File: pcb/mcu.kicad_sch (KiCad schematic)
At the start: 28 parts, among them J1 CON_SAMTEC_14P_2R_1m27_P_KEY_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, U3 IC_MCU_STM32F100C4T6B_48LQFP, X1 XTAL_8M_20PPM_18pF_ECS-80-18-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, X2 XTAL_32K768_10PPM_7pF_ECS-.32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

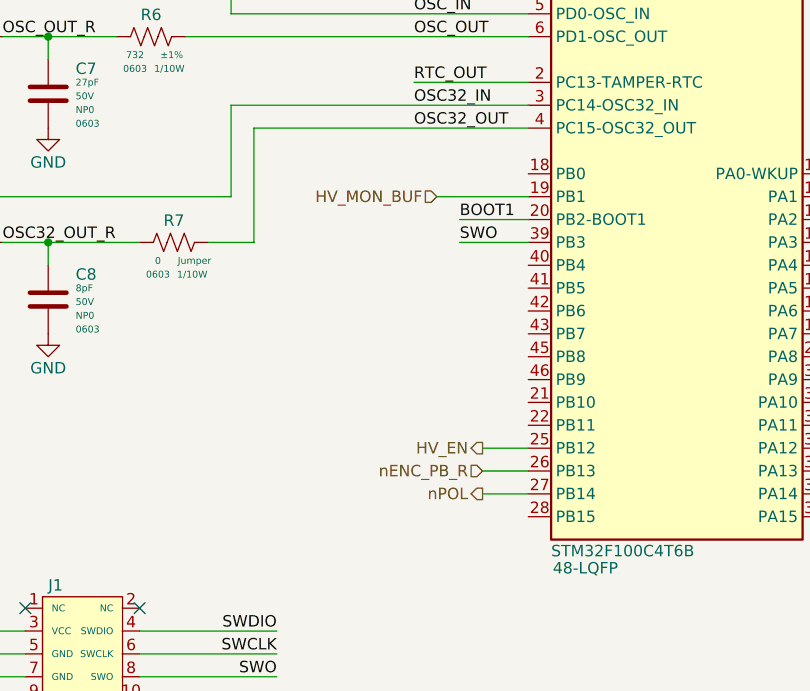
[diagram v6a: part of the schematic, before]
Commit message: Added 12V and 180V sense lines
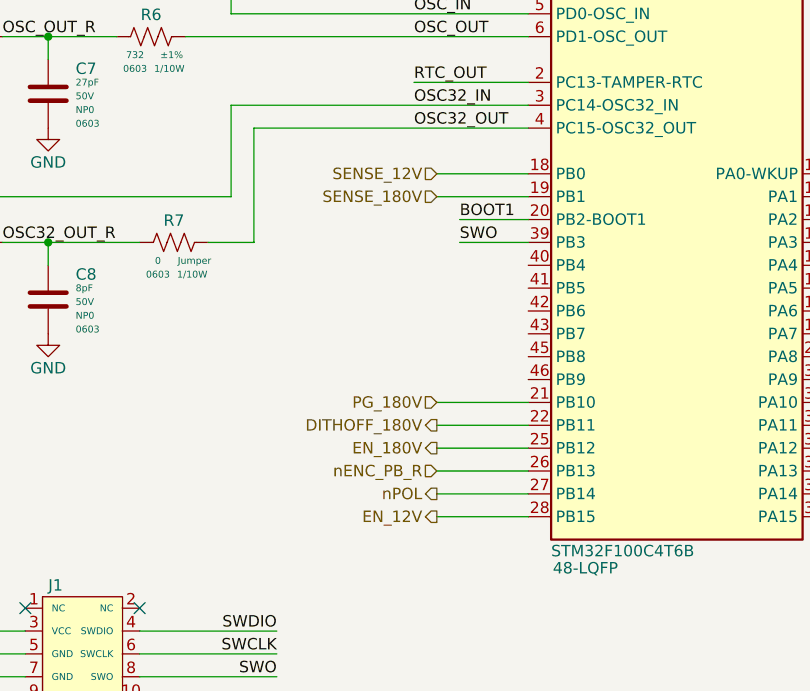
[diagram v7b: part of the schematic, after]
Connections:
- net SENSE_12V: now reaches U3.18 (PB0)
- net PG_180V: now reaches U3.21 (PB10)
- net DITHOFF_180V: now reaches U3.22 (PB11)
- net EN_12V: now reaches U3.28 (PB15)
- net HV_EN renamed EN_180V
- net HV_MON_BUF renamed SENSE_180V
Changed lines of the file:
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@@
+    (stroke (width 0) (type default) (color 0 0 0 0))
+  )
+  (wire (pts (xy 91.44 149.86) (xy 101.6 149.86))
     (stroke (width 0) (type default) (color 0 0 0 0))
   )
@@
     (stroke (width 0) (type default) (color 0 0 0 0))
   )
-  (wire (pts (xy 96.52 142.24) (xy 101.6 142.24))
+  (wire (pts (xy 91.44 142.24) (xy 101.6 142.24))
     (stroke (width 0) (type default) (color 0 0 0 0))
   )
@@
     (stroke (width 0) (type default) (color 0 0 0 0))
   )
+  (wire (pts (xy 101.6 139.7) (xy 91.44 139.7))
+    (stroke (width 0) (type default) (color 0 0 0 0))
+  )
+  (wire (pts (xy 101.6 111.76) (xy 91.44 111.76))
+    (stroke (width 0) (type default) (color 0 0 0 0))
+  )
   (wire (pts (xy 27.94 165.1) (xy 45.72 165.1))
     (stroke (width 0) (type default) (color 0 0 0 0))
@@
     (stroke (width 0) (type default) (color 0 0 0 0))
   )
-  (wire (pts (xy 96.52 147.32) (xy 101.6 147.32))
+  (wire (pts (xy 91.44 147.32) (xy 101.6 147.32))
     (stroke (width 0) (type default) (color 0 0 0 0))
   )
@@
     (stroke (width 0) (type default) (color 0 0 0 0))
   )
+  (wire (pts (xy 101.6 137.16) (xy 91.44 137.16))
+    (stroke (width 0) (type default) (color 0 0 0 0))
+  )
   (wire (pts (xy 27.94 167.64) (xy 45.72 167.64))
     (stroke (width 0) (type default) (color 0 0 0 0))
@@
     (stroke (width 0) (type default) (color 0 0 0 0))
   )
-  (wire (pts (xy 96.52 144.78) (xy 101.6 144.78))
+  (wire (pts (xy 91.44 144.78) (xy 101.6 144.78))
     (stroke (width 0) (type default) (color 0 0 0 0))
   )
@@
     (effects (font (size 1.27 1.27)) (justify left))
   )
+  (hierarchical_label "EN_12V" (shape output) (at 91.44 149.86 180)
+    (effects (font (size 1.27 1.27)) (justify right))
+  )
+  (hierarchical_label "SENSE_12V" (shape input) (at 91.44 111.76 180)
+    (effects (font (size 1.27 1.27)) (justify right))
+  )
   (hierarchical_label "PWM_nBL" (shape output) (at 152.4 127 0)
     (effects (font (size 1.27 1.27)) (justify left))
   )
-  (hierarchical_label "HV_EN" (shape output) (at 96.52 142.24 180)
+  (hierarchical_label "EN_180V" (shape output) (at 91.44 142.24 180)
     (effects (font (size 1.27 1.27)) (justify right))
   )
@@
     (effects (font (size 1.27 1.27)) (justify left))
   )
-  (hierarchical_label "HV_MON_BUF" (shape input) (at 91.44 114.3 180)
-    (effects (font (size 1.27 1.27)) (justify right))
-  )
-  (hierarchical_label "nPOL" (shape output) (at 96.52 147.32 180)
+  (hierarchical_label "SENSE_180V" (shape input) (at 91.44 114.3 180)
+    (effects (font (size 1.27 1.27)) (justify right))
+  )
+  (hierarchical_label "nPOL" (shape output) (at 91.44 147.32 180)
+    (effects (font (size 1.27 1.27)) (justify right))
+  )
+  (hierarchical_label "DITHOFF_180V" (shape output) (at 91.44 139.7 180)
     (effects (font (size 1.27 1.27)) (justify right))
   )
@@
     (effects (font (size 1.27 1.27)) (justify left))
   )
+  (hierarchical_label "PG_180V" (shape input) (at 91.44 137.16 180)
+    (effects (font (size 1.27 1.27)) (justify right))
+  )
   (hierarchical_label "UART_BL_RX" (shape input) (at 152.4 137.16 0)
     (effects (font (size 1.27 1.27)) (justify left))
   )
-  (hierarchical_label "nENC_PB_R" (shape input) (at 96.52 144.78 180)
-    (effects (font (size 1.27 1.27)) (justify right))
-  )
+  (hierarchical_label "nENC_PB_R" (shape input) (at 91.44 144.78 180)
+    (effects (font (size 1.27 1.27)) (justify right))
+  )

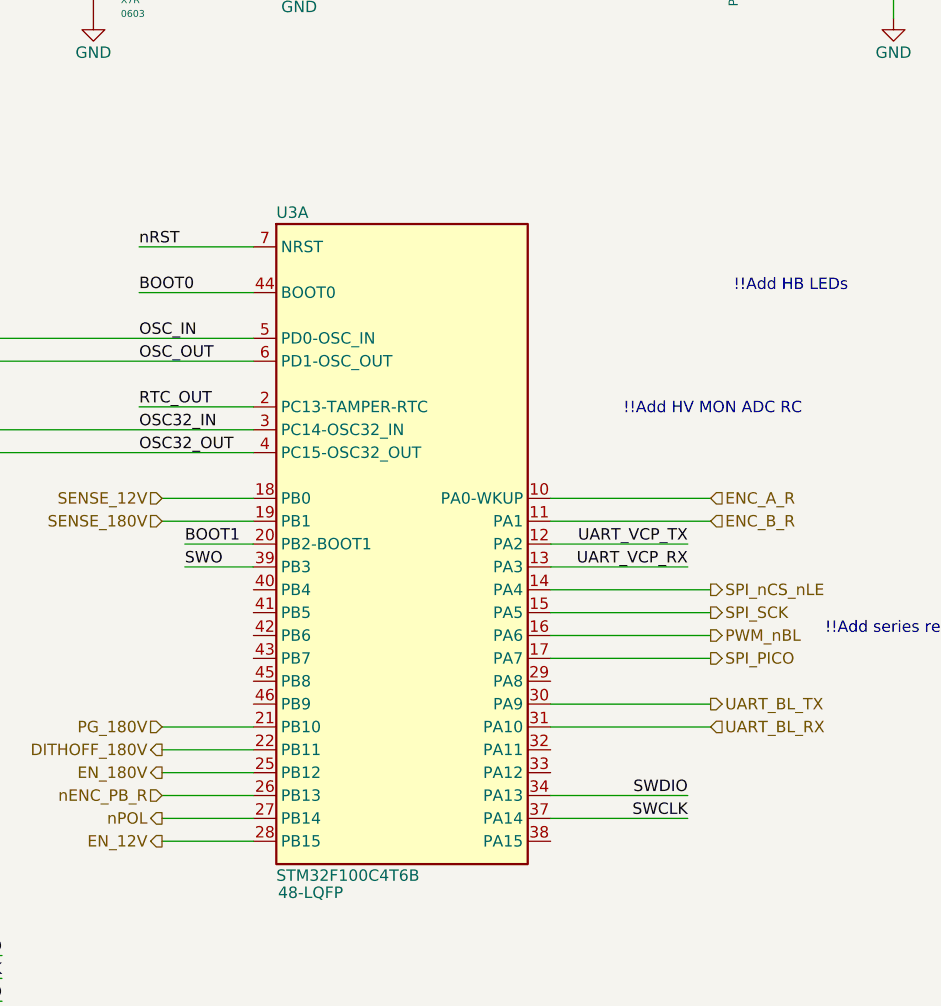
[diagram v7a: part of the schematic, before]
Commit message: Updated ftdi page
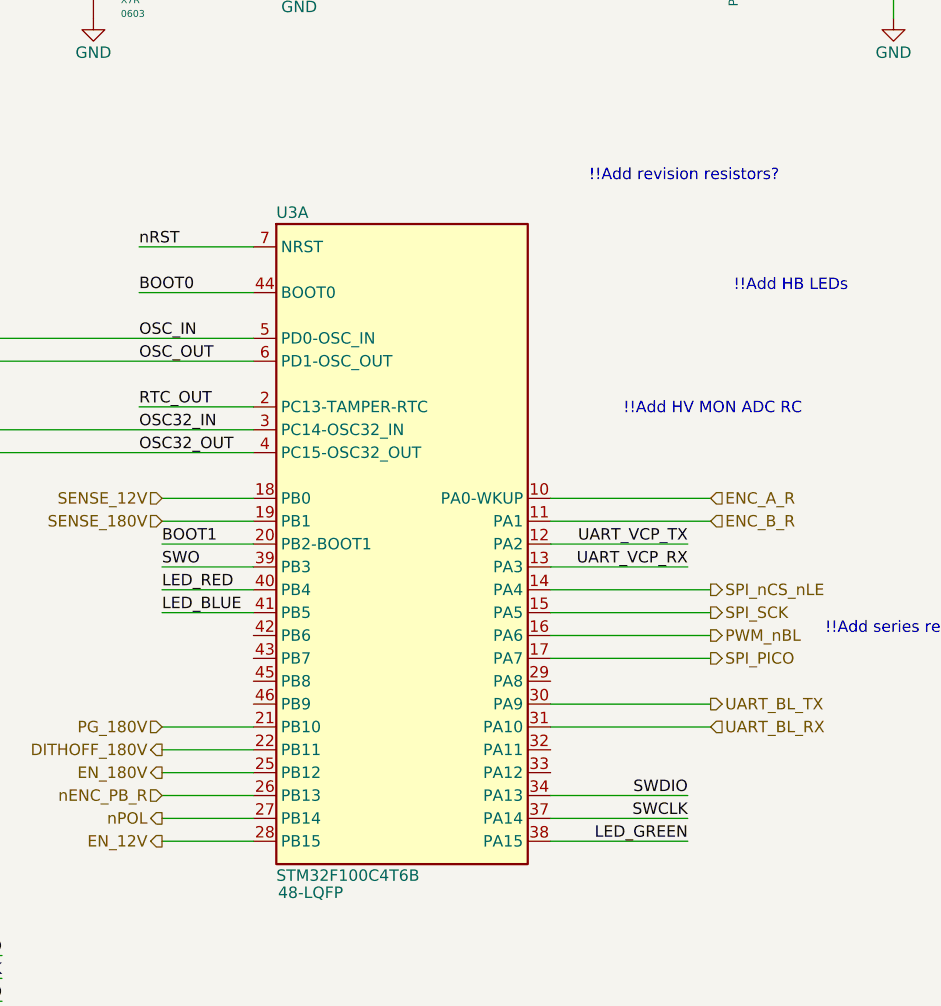
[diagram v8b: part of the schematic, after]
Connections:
- net LED_GREEN: now reaches U3.38 (PA15)
- net LED_RED: now reaches U3.40 (PB4)
- net LED_BLUE: now reaches U3.41 (PB5)
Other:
- note added: "!!Add revision resistors?"
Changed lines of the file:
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@@
 (kicad_sch (version 20211123) (generator eeschema)
   (paper "A4")
+  (title_block
+    (date "2024-05-14")
+    (rev "1")
+  )
   (junction (at 83.82 48.26) (diameter 0) (color 0 0 0 0)
   )
@@
     (stroke (width 0) (type default) (color 0 0 0 0))
   )
-  (wire (pts (xy 93.98 116.84) (xy 101.6 116.84))
-    (stroke (width 0) (type default) (color 0 0 0 0))
-  )
   (wire (pts (xy 58.42 48.26) (xy 63.5 48.26))
     (stroke (width 0) (type default) (color 0 0 0 0))
@@
     (stroke (width 0) (type default) (color 0 0 0 0))
   )
+  (wire (pts (xy 134.62 149.86) (xy 149.86 149.86))
+    (stroke (width 0) (type default) (color 0 0 0 0))
+  )
   (wire (pts (xy 190.5 116.84) (xy 190.5 119.38))
     (stroke (width 0) (type default) (color 0 0 0 0))
@@
     (stroke (width 0) (type default) (color 0 0 0 0))
   )
+  (wire (pts (xy 91.44 121.92) (xy 101.6 121.92))
+    (stroke (width 0) (type default) (color 0 0 0 0))
+  )
   (wire (pts (xy 134.62 111.76) (xy 152.4 111.76))
     (stroke (width 0) (type default) (color 0 0 0 0))
@@
     (stroke (width 0) (type default) (color 0 0 0 0))
   )
+  (wire (pts (xy 91.44 124.46) (xy 101.6 124.46))
+    (stroke (width 0) (type default) (color 0 0 0 0))
+  )
   (wire (pts (xy 200.66 116.84) (xy 210.82 116.84))
     (stroke (width 0) (type default) (color 0 0 0 0))
@@
     (stroke (width 0) (type default) (color 0 0 0 0))
   )
+  (wire (pts (xy 91.44 116.84) (xy 101.6 116.84))
+    (stroke (width 0) (type default) (color 0 0 0 0))
+  )
   (wire (pts (xy 200.66 104.14) (xy 210.82 104.14))
     (stroke (width 0) (type default) (color 0 0 0 0))
@@
     (stroke (width 0) (type default) (color 0 0 0 0))
   )
+  (wire (pts (xy 91.44 119.38) (xy 101.6 119.38))
+    (stroke (width 0) (type default) (color 0 0 0 0))
+  )
   (wire (pts (xy 210.82 104.14) (xy 220.98 104.14))
     (stroke (width 0) (type default) (color 0 0 0 0))
@@
   )
   (wire (pts (xy 27.94 167.64) (xy 45.72 167.64))
-    (stroke (width 0) (type default) (color 0 0 0 0))
-  )
-  (wire (pts (xy 93.98 119.38) (xy 101.6 119.38))
     (stroke (width 0) (type default) (color 0 0 0 0))
   )
@@
     (effects (font (size 1.27 1.27) (thickness 0.254) bold) (justify left bottom))
   )
+  (text "!!Add revision resistors?\n\n" (at 160.02 78.74 180)
+    (effects (font (size 1.27 1.27)) (justify right bottom))
+  )
   (text "BOOT0" (at 81.28 27.94 0)
     (effects (font (size 1.27 1.27) (thickness 0.254) bold) (justify left bottom))
@@
     (effects (font (size 1.27 1.27)) (justify left bottom))
   )
+  (label "LED_BLUE" (at 91.44 124.46 0)
+    (effects (font (size 1.27 1.27)) (justify left bottom))
+  )
   (label "SWO" (at 73.66 167.64 180)
     (effects (font (size 1.27 1.27)) (justify right bottom))
@@
     (effects (font (size 1.27 1.27)) (justify left bottom))
   )
-  (label "SWO" (at 93.98 119.38 0)
+  (label "SWO" (at 91.44 119.38 0)
     (effects (font (size 1.27 1.27)) (justify left bottom))
   )
@@
     (effects (font (size 1.27 1.27)) (justify left bottom))
   )
+  (label "LED_GREEN" (at 149.86 149.86 180)
+    (effects (font (size 1.27 1.27)) (justify right bottom))
+  )
   (label "RTC_OUT" (at 88.9 101.6 0)
     (effects (font (size 1.27 1.27)) (justify left bottom))
@@
     (effects (font (size 1.27 1.27)) (justify right bottom))
   )
+  (label "LED_RED" (at 91.44 121.92 0)
+    (effects (font (size 1.27 1.27)) (justify left bottom))
+  )
   (label "OSC32_IN" (at 88.9 104.14 0)
     (effects (font (size 1.27 1.27)) (justify left bottom))
@@
     (effects (font (size 1.27 1.27)) (justify left bottom))
   )
-  (label "BOOT1" (at 93.98 116.84 0)
-    (effects (font (size 1.27 1.27)) (justify left bottom))
-  )
+  (label "BOOT1" (at 91.44 116.84 0)
+    (effects (font (size 1.27 1.27)) (justify left bottom))
+  )
